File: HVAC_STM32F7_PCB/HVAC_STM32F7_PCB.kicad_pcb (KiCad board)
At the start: 4 copper layers, 190 x 122.6 mm, 98 parts, among them J1 DC_Jack_5.5x2.1mm, J10 OUT_Signal_connector, J11 OUT_Signal_connector, J12 OUT_Signal_connector, J13 OUT_Signal_connector, J14 Signal_connector, J15 Signal_connector, J16 Signal_connector, J17 Signal_connector, J2 Signal_connector, J3 Signal_connector, J4 Signal_connector, J5 Signal_connector, J6 OUT_Signal_connector, J7 OUT_Signal_connector, J8 OUT_Signal_connector, J9 OUT_Signal_connector, Q1 IRLML9301, SW1 SLW-1276864-4A-D, U1 LM2596S-5, U2 LM2596S-3.3, U3 DAC7568IAPW, U5 TLV9304xPW, U6 TLV9304xPW, U7 ADS8688

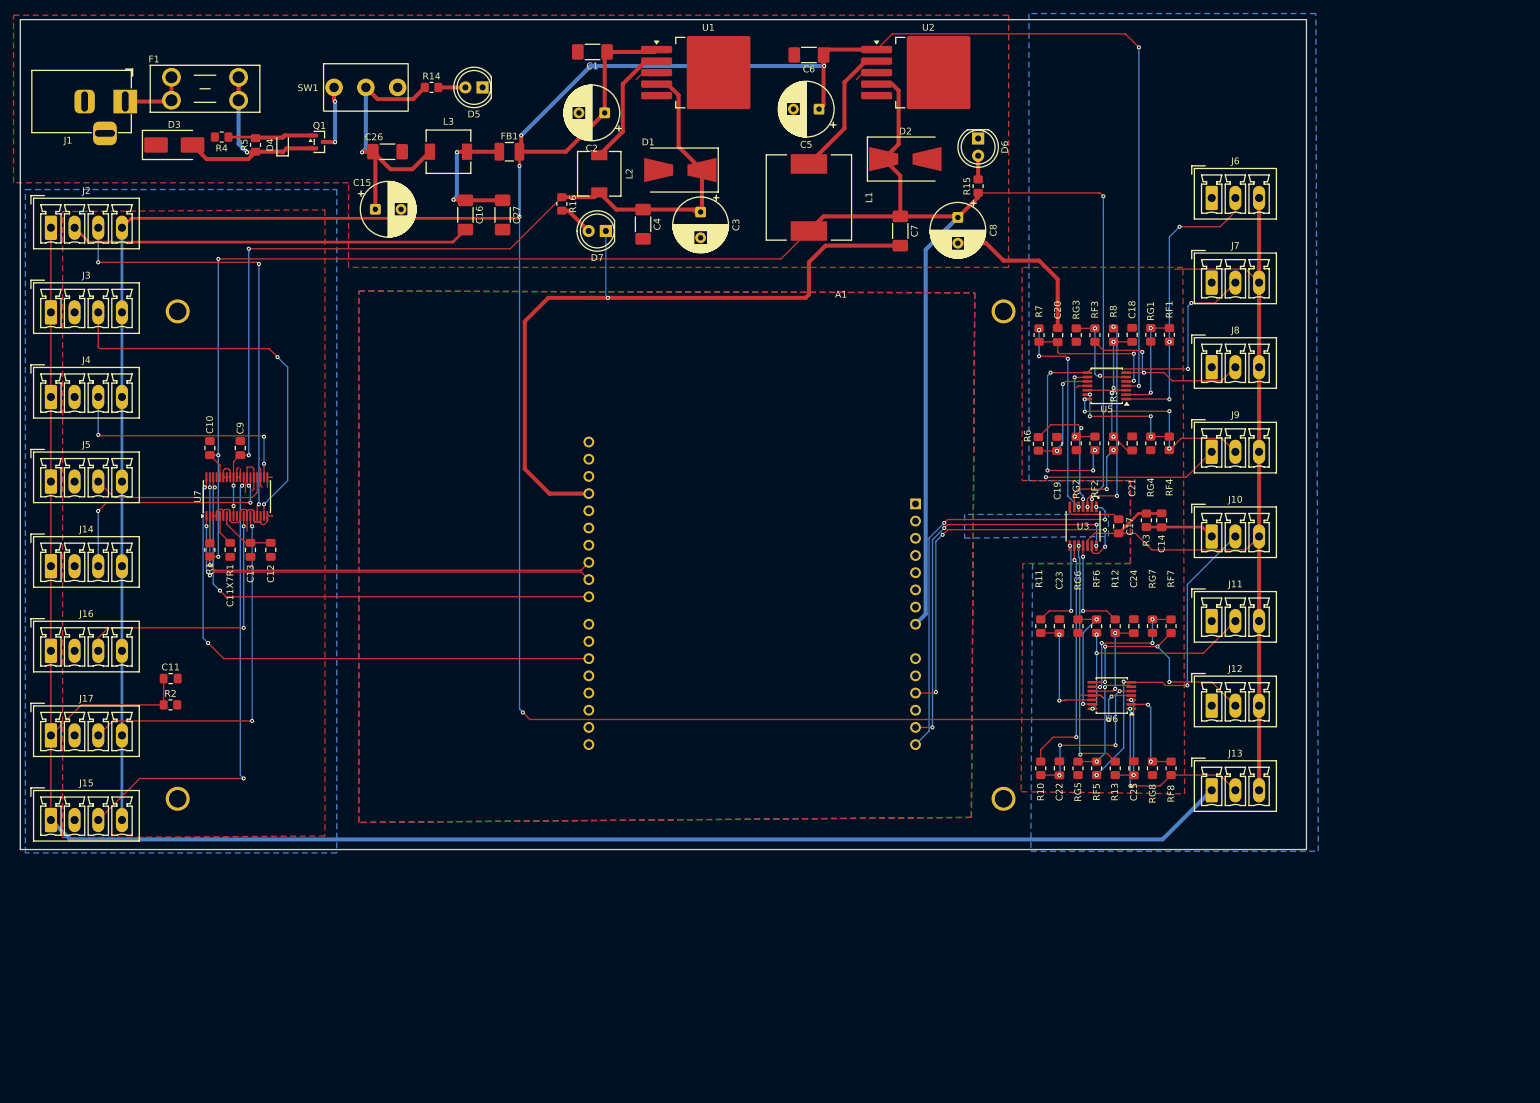
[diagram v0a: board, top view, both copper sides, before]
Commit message: ADD: walka z przestawianiem konektorów wejściowych i wyjściowych, TODO: dokończyć łączenie wejściowego ADC
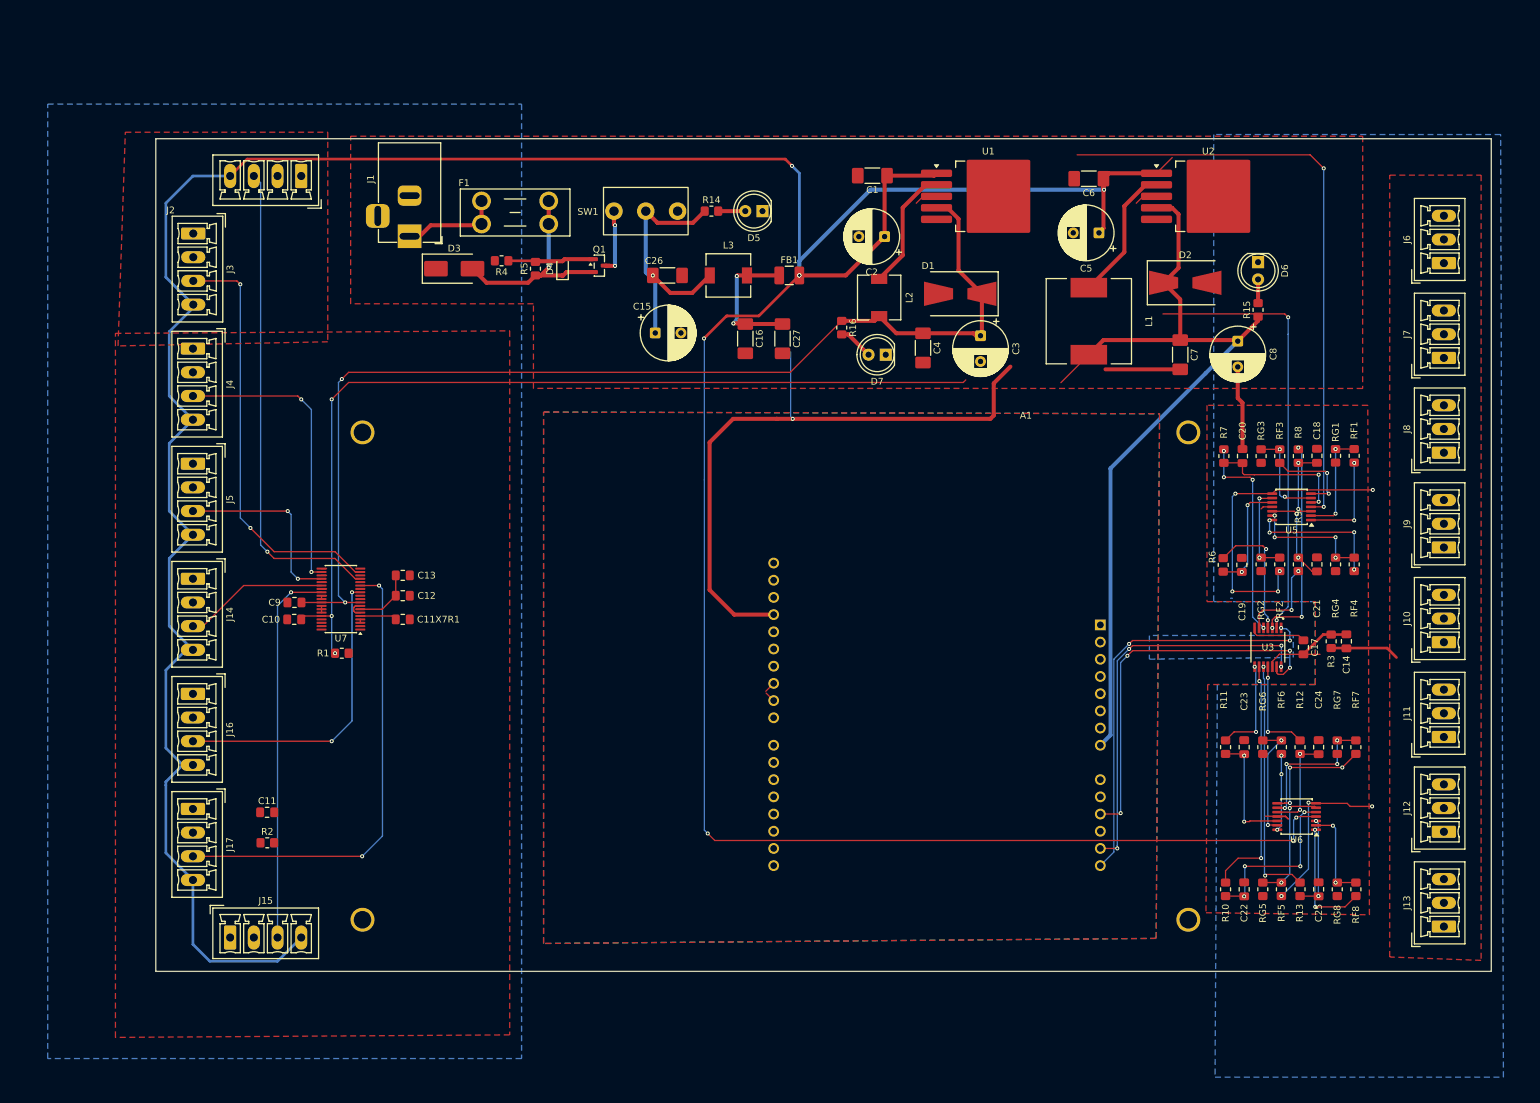
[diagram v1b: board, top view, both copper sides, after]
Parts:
- moved F1 49.3 mm to (82.1, 40.2)
- moved J1 46.5 mm to (71.5, 45.4), turned to -90 degrees
- moved SW1 45.2 mm to (106.4, 41.7)
- moved C1 45.2 mm to (139.9, 36.5)
- moved C16 45.2 mm to (121.1, 60.5)
- moved C2 45.2 mm to (141.7, 45.5)
- moved C27 45.2 mm to (126.6, 60.5)
- moved L1 45.2 mm to (171.8, 58.0)
- moved L2 45.2 mm to (140.9, 54.5)
- moved Q1 45.2 mm to (99.5, 49.7)
- moved C15 45.2 mm to (107.8, 59.7)
- moved C26 45.2 mm to (109.6, 51.2)
- moved C3 45.2 mm to (155.8, 60.1)
- moved C4 45.2 mm to (147.3, 61.9)
- moved C5 45.2 mm to (173.3, 44.9)
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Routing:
- net GNDA: track 322.2 -> 10.5 mm, vias 1 -> 0
- net GND: track 384.8 -> 158.1 mm
- net +24V: track 517.1 -> 636.6 mm, vias 9 -> 10
- net Net-(A1-D5): track 82.2 -> 0.00 mm, vias 2 -> 0
- net Net-(A1-D8): track 72.2 -> 0.00 mm, vias 2 -> 0
- net Net-(A1-D10): track 69.8 -> 1.65 mm, vias 2 -> 0
- net Net-(A1-D9): track 65.6 -> 1.58 mm, vias 2 -> 0
- net +5V: track 135.3 -> 164.4 mm, vias 4 -> 2
- net Net-(J6-GND): track 43.7 -> 14.9 mm, vias 3 -> 2
- net Net-(J10-GND): track 50.0 -> 25.1 mm
- net Net-(J11-GND): track 33.9 -> 11.5 mm
- net Net-(J7-GND): track 62.7 -> 45.0 mm, vias 6 -> 5
- net Net-(J12-GND): track 34.9 -> 17.7 mm, vias 4 -> 3
- net Net-(J17-SIG): track 54.0 -> 69.2 mm
- net Net-(J8-GND): track 28.2 -> 13.4 mm
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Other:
- board size 190 x 122.6 mm -> 197.3 x 123 mm

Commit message: add: ADC podłączone elegancko, separacja mas sygnałów wejściowych, TODO: DRC
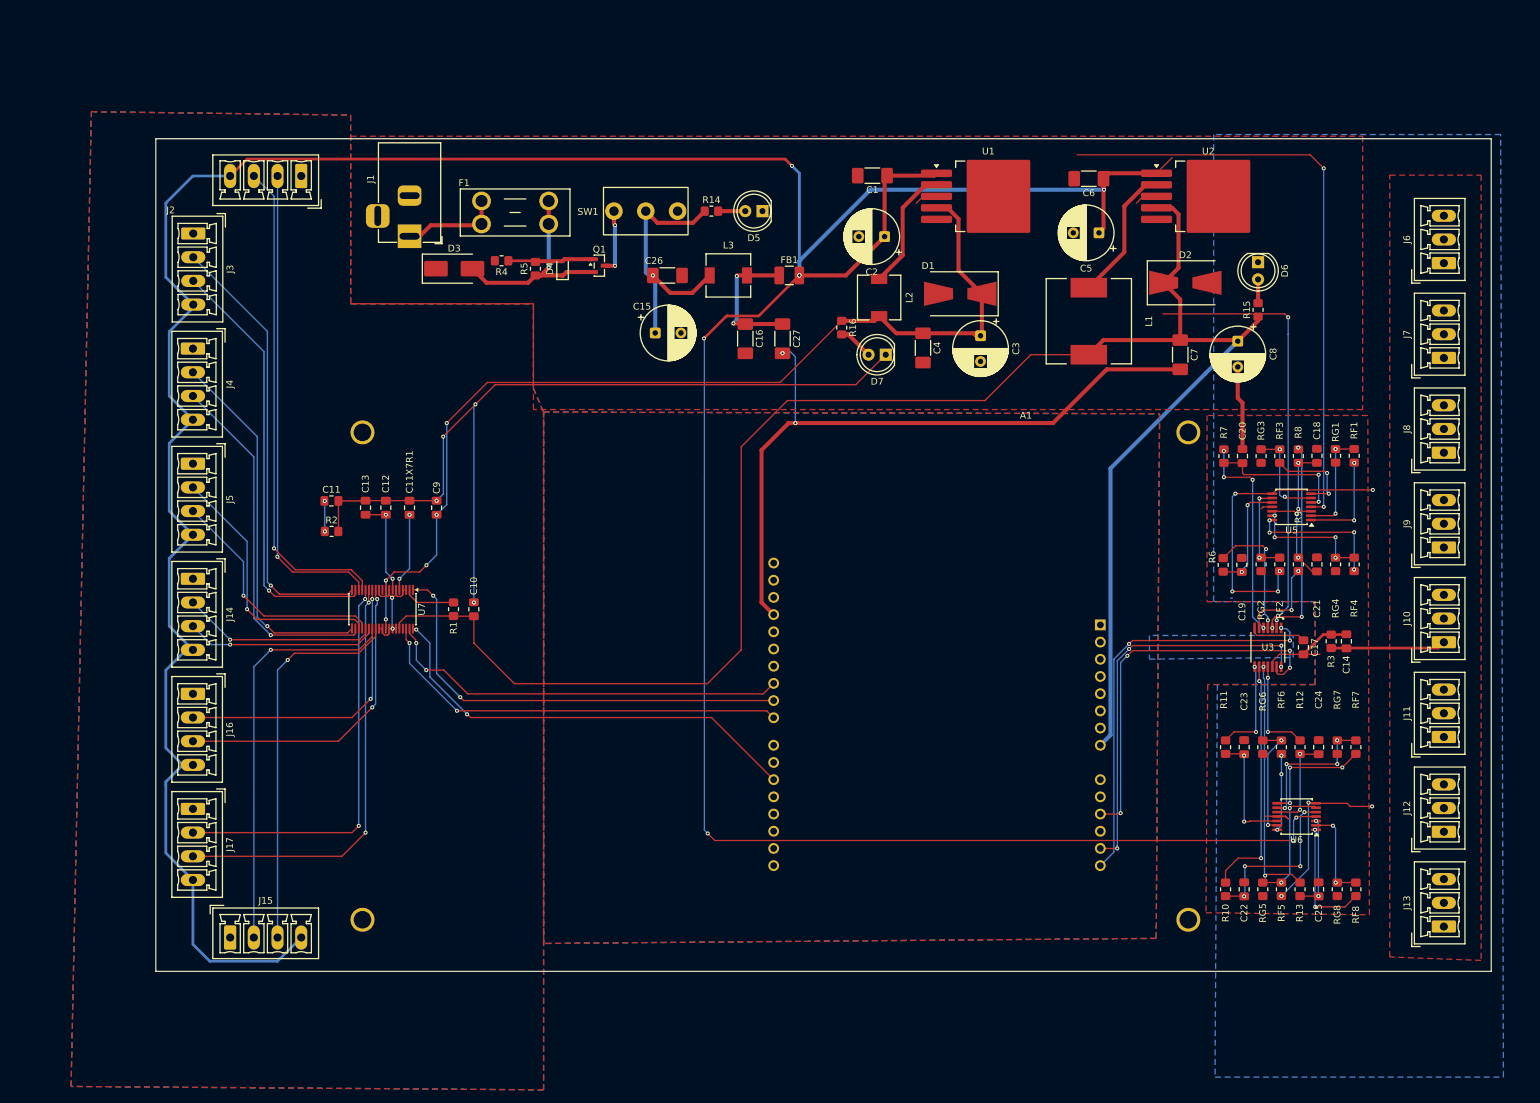
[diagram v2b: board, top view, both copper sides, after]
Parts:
- moved C11 47.0 mm to (60.0, 84.5)
- moved R2 47.0 mm to (60.0, 89.0)
- moved C10 26.6 mm to (81.0, 100.5), turned to 90 degrees
- moved C9 25.2 mm to (75.5, 85.5), turned to -90 degrees
- moved R1 17.7 mm to (78.0, 100.5), turned to 90 degrees
- moved C11X7R1 16.5 mm to (71.5, 85.5), turned to 90 degrees
- moved C12 13.2 mm to (68.0, 85.5), turned to 90 degrees
- moved C13 11.4 mm to (65.0, 85.5), turned to 90 degrees
- moved U7 6.32 mm to (67.5, 100.5), turned to -90 degrees
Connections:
- J14 pad 2: GND -> Net-(J14-GND)
- J15 pad 2: GND -> Net-(J15-GND)
- J16 pad 2: GND -> Net-(J16-GND)
- J17 pad 2: GND -> Net-(J17-GND)
- J2 pad 2: GND -> Net-(J2-GND)
- J3 pad 2: GND -> Net-(J3-GND)
- J4 pad 2: GND -> Net-(J4-GND)
- J5 pad 2: GND -> Net-(J5-GND)
- U7 pad 13: GND -> Net-(J16-GND)
- U7 pad 15: GND -> Net-(J17-GND)
- U7 pad 17: GND -> Net-(J2-GND)
- U7 pad 19: GND -> Net-(J3-GND)
- U7 pad 20: GND -> Net-(J4-GND)
- U7 pad 22: GND -> Net-(J5-GND)
- U7 pad 24: GND -> Net-(J14-GND)
- U7 pad 26: GND -> Net-(J15-GND)
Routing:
- net GND: track 158.1 -> 293.0 mm, vias 1 -> 8
- net Net-(J2-GND): track 0.00 -> 71.0 mm, vias 0 -> 1
- net Net-(J3-GND): track 0.00 -> 66.0 mm, vias 0 -> 1
- net Net-(A1-D5): track 0.00 -> 65.5 mm, vias 0 -> 2
- net Net-(A1-D9): track 1.58 -> 66.7 mm, vias 0 -> 2
- net Net-(A1-D8): track 0.00 -> 62.5 mm, vias 0 -> 2
- net Net-(J15-GND): track 0.00 -> 60.5 mm, vias 0 -> 1
- net Net-(J17-GND): track 0.00 -> 60.2 mm, vias 0 -> 2
- net Net-(A1-D10): track 1.65 -> 60.6 mm, vias 0 -> 2
- net Net-(J4-GND): track 0.00 -> 56.1 mm, vias 0 -> 1
- net Net-(J16-GND): track 0.00 -> 43.6 mm, vias 0 -> 2
- net Net-(J5-GND): track 0.00 -> 39.4 mm, vias 0 -> 1
- net Net-(J14-GND): track 0.00 -> 28.9 mm, vias 0 -> 1
- net +5V: track 164.4 -> 147.0 mm, vias 2 -> 5
- net GNDA: track 10.5 -> 21.8 mm, vias 0 -> 2
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- added copper zone on F.Cu, net GNDA

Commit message: zabawy z grubościami ścierzek
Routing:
- net GNDA: track 21.8 -> 204.4 mm, vias 2 -> 3
- net Net-(J6-GND): track 14.9 -> 60.0 mm, vias 2 -> 4
- net Net-(J10-GND): track 25.1 -> 63.3 mm, vias 3 -> 4
- net Net-(J7-GND): track 45.0 -> 77.3 mm, vias 5 -> 6
- net Net-(J11-GND): track 11.5 -> 41.2 mm, vias 3 -> 4
- net Net-(J8-GND): track 13.4 -> 36.6 mm, vias 2 -> 4
- net Net-(J12-GND): track 17.7 -> 39.0 mm, vias 3 -> 4
- net +3.3V: track 333.5 -> 319.6 mm
- net +24V: track 636.6 -> 622.7 mm
- net Net-(J9-GND): track 19.7 -> 33.5 mm
- net Net-(J13-GND): track 18.1 -> 31.5 mm
- net GND: track 293.0 -> 305.0 mm
- net Net-(J2-GND): track 71.0 -> 71.7 mm

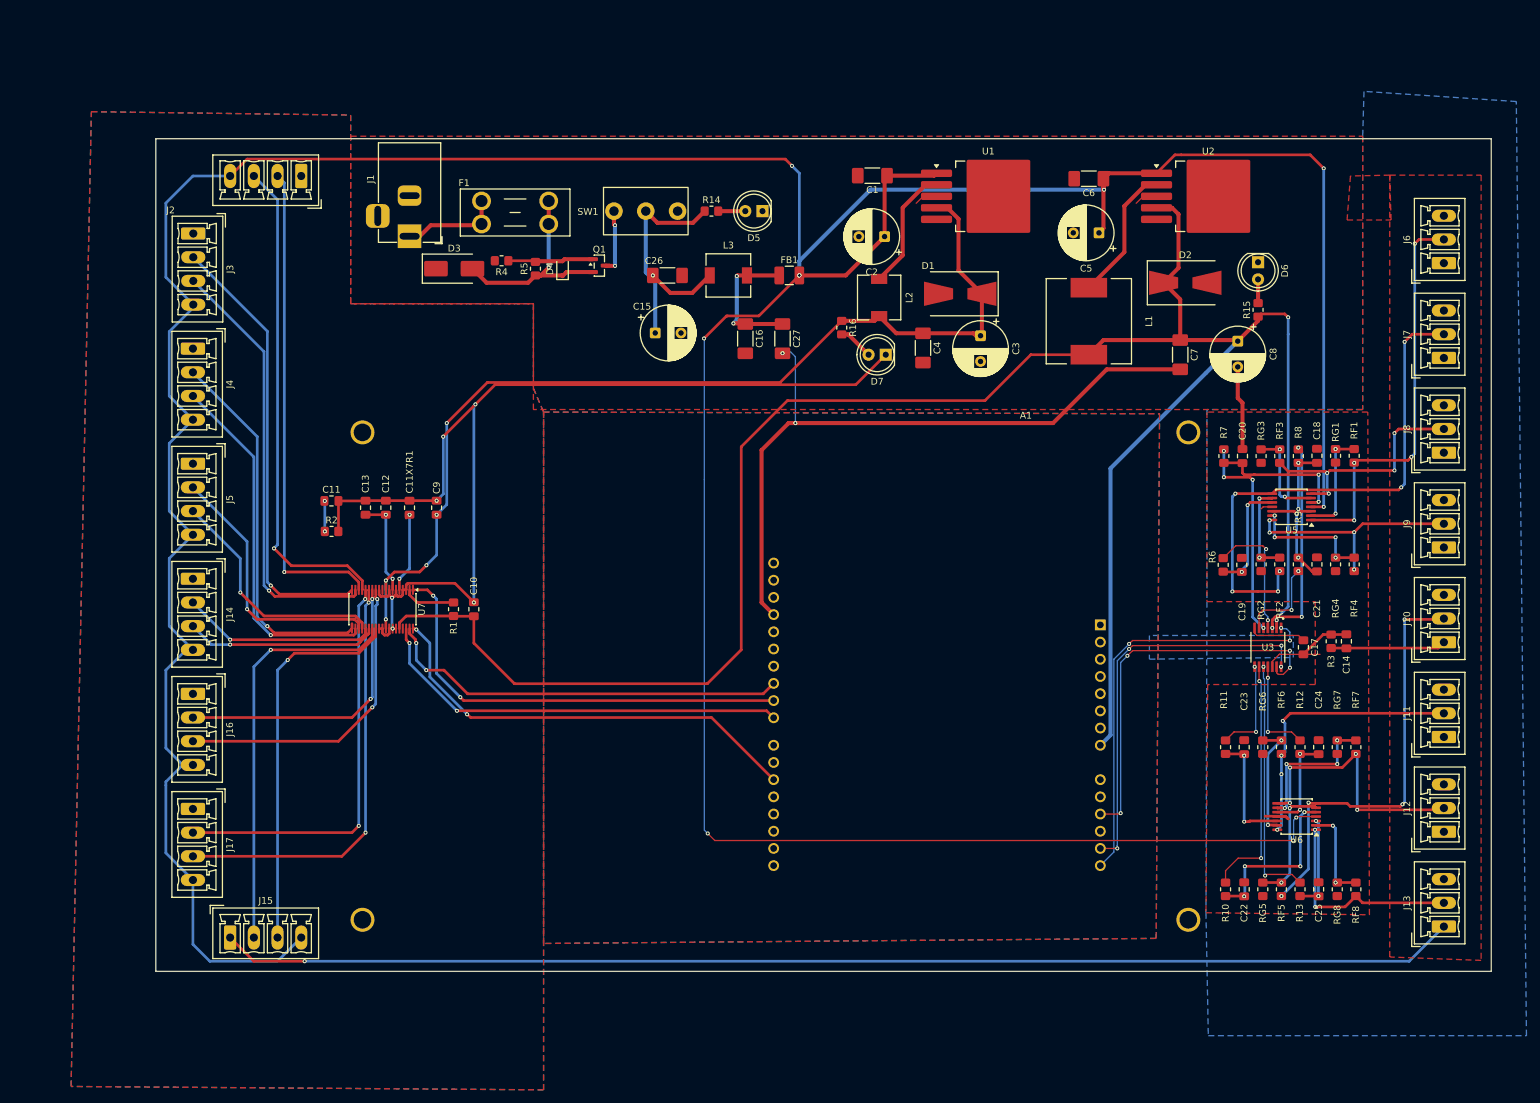
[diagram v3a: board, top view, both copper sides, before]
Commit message: ADD naprawione DRC, TODO last check, filkscreen text
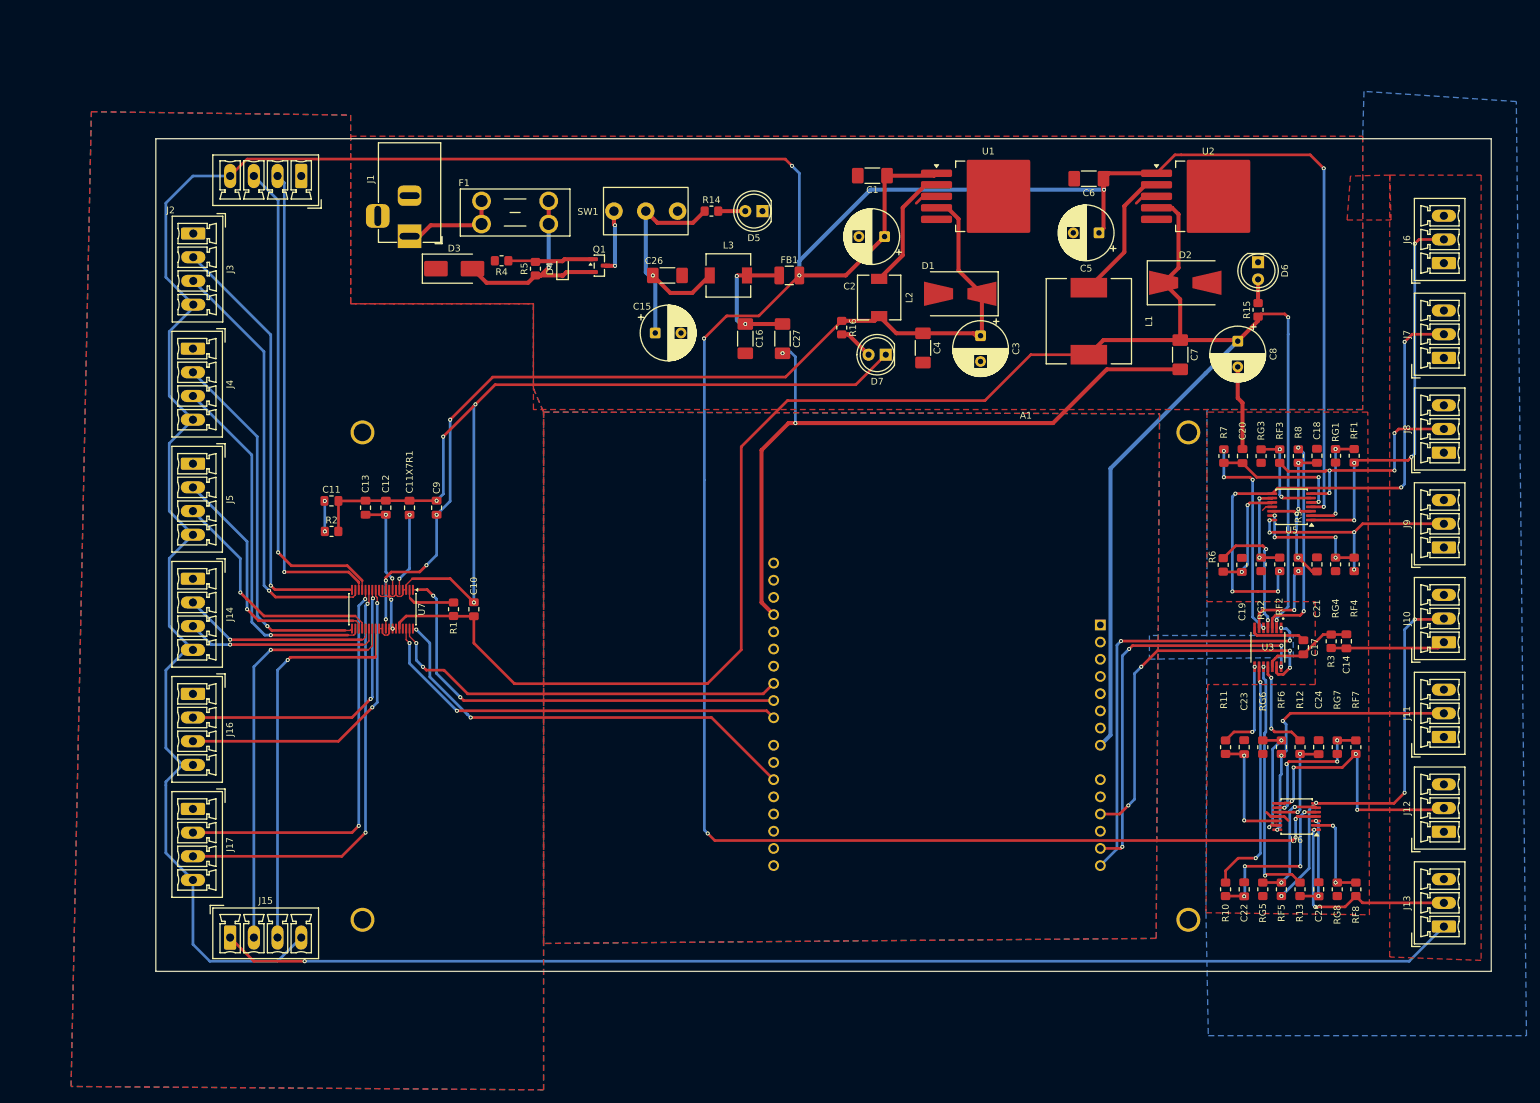
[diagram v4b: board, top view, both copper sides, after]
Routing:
- net Net-(J10-GND): track 63.3 -> 60.3 mm
- net MOSI_OUT: track 56.9 -> 54.8 mm
- net GND: track 305.0 -> 303.1 mm
- net Net-(J15-SIG): track 57.2 -> 59.0 mm
- net Net-(J4-GND): track 56.1 -> 54.9 mm
- net Net-(U5B-+): track 20.8 -> 19.7 mm
- net Net-(C16-Pad1): track 20.8 -> 19.8 mm
- net NSS_OUT: track 61.3 -> 62.3 mm
- net Net-(J15-GND): track 60.5 -> 61.3 mm
- net Net-(J14-SIG): track 28.5 -> 29.2 mm
- net Net-(U3-VOUTB): track 14.9 -> 14.3 mm
- net Net-(U3-VOUTF): track 36.2 -> 35.6 mm
- net Net-(J3-GND): track 66.0 -> 65.5 mm
- net Net-(J4-SIG): track 53.4 -> 53.9 mm
- net Net-(J11-GND): track 41.2 -> 41.3 mm, vias 4 -> 3
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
